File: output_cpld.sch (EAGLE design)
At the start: 40 parts, among them IC1 LM2852Y-3V3, J1 MAGJACK, U1 ONION-OMEGA2

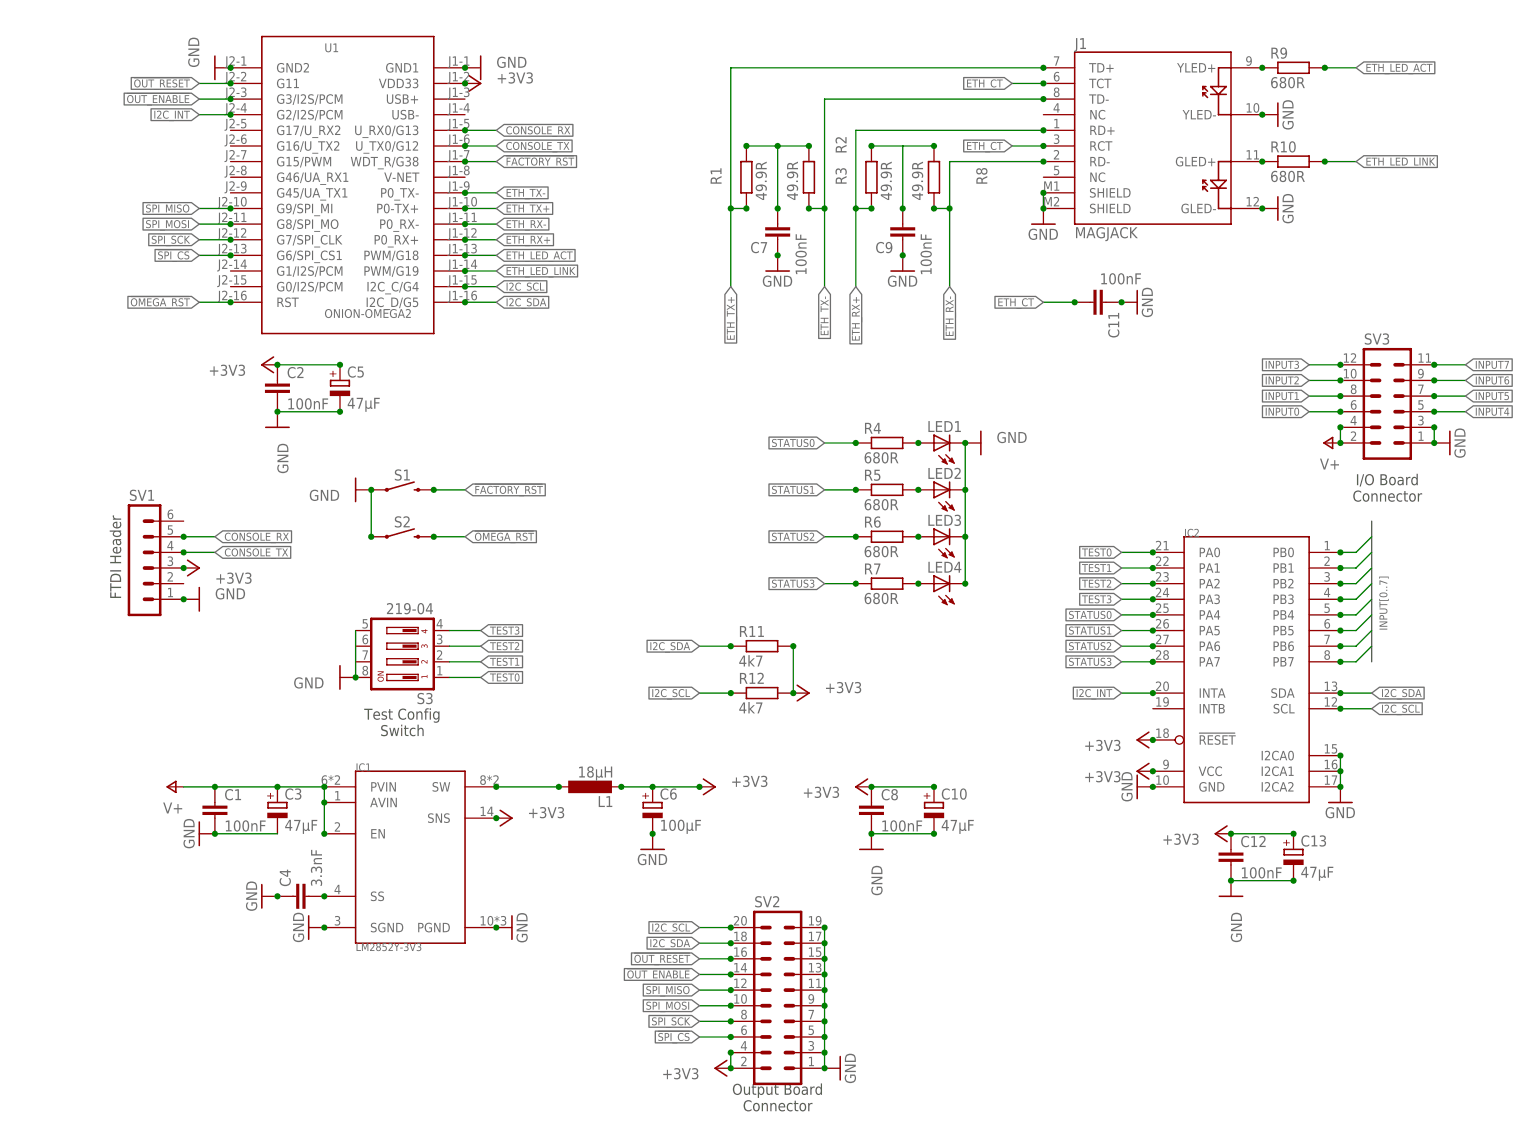
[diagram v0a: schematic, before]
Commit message: moved output CPLD to its own schematic/board
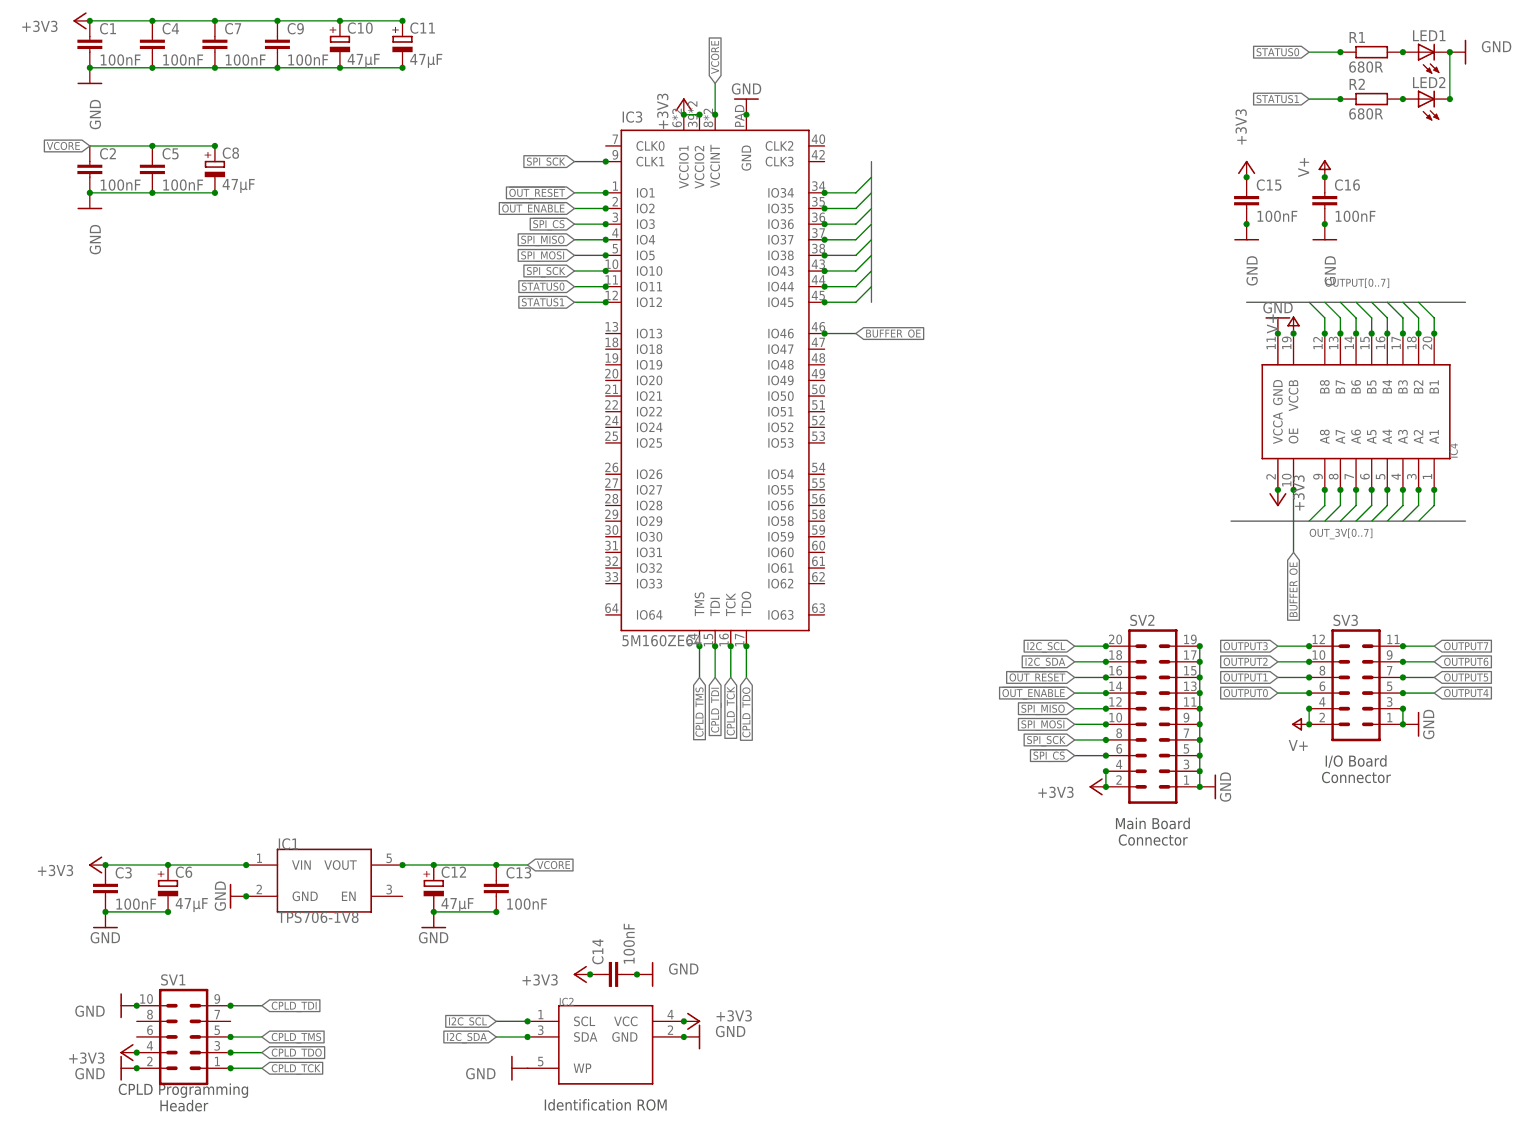
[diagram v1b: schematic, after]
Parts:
- removed J1: MAGJACK, SparkFun-Connectors:MAGJACK
- removed L1: 18µH, lichtenstein_onion:SRR1050A
- removed LED3, LED4: (no value), led:LEDCHIPLED_1206
- removed R10, R4, R5, R6, R7, R9: 680R, rcl:R-EU_M0805
- removed R11, R12: 4k7, rcl:R-EU_M0805
- removed R3, R8: 49.9R, rcl:R-EU_M0805
- removed S1, S2: MOMENTARY-SWITCH-SPST-PTH-6.0MM, SparkFun-Switches:MOMENTARY-SWITCH-SPST-PTH-6.0MM
- removed S3: 219-04, switch-dil:219-04
- removed U1: ONION-OMEGA2, lichtenstein_onion:ONION-OMEGA2
- added C14, C15, C16: 100nF, rcl:C-EUC0805
- added IC3: 5M160ZE64, lichtenstein_onion:5M160ZE64
- added IC4: (no value), lichtenstein_onion:TXB0108TSSOP20
- C11, C12, C8: value 100nF -> 47µF; device rcl:C-EUC0805 -> rcl:CPOL-EUCT6032; MOUSER (none) -> 581-NOSD107M006
- C13, C3, C5: value 47µF -> 100nF; device rcl:CPOL-EUCT6032 -> rcl:C-EUC0805; MOUSER 581-NOSD107M006 -> (none)
- C4: value 3.3nF -> 100nF
- C6: value 100µF -> 47µF; device rcl:CPOL-EUSMCD -> rcl:CPOL-EUCT6032
- IC1: value LM2852Y-3V3 -> TPS706-1V8; device lichtenstein_onion:LM2852HTSSOP14 -> lichtenstein_onion:TPS706SOT23-5
- IC2: device lichtenstein_onion:MCP23017SSOP28 -> lichtenstein_onion:AT24C02D
- R1, R2: value 49.9R -> 680R
- SV1: device con-lstb:MA06-1 -> con-lstb:MA05-2
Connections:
- removed net !FACTORY_RST: S1.2, U1.WDT_R/G38
- removed net !OMEGA_RST: S2.2, U1.RST
- removed net CONSOLE_RX: SV1.5, U1.U_RX0/G13
- removed net CONSOLE_TX: SV1.4, U1.U_TX0/G12
- removed net ETH_CT: C11.2, J1.RCT, J1.TCT
- removed net ETH_LED_ACT: R9.2, U1.PWM/G18
- removed net ETH_LED_LINK: R10.2, U1.PWM/G19
- removed net ETH_RX+: J1.RD+, R3.1, U1.P0_RX+
- removed net ETH_RX-: J1.RD-, R8.1, U1.P0_RX-
- removed net ETH_TX+: J1.TD+, R1.1, U1.P0-TX+
- removed net ETH_TX-: J1.TD-, R2.1, U1.P0_TX-
- removed net I2C_INT: IC2.INTA, U1.G2/I2S/PCM
- removed net INPUT0: IC2.PB0, SV3.6
- removed net INPUT1: IC2.PB1, SV3.8
- removed net INPUT2: IC2.PB2, SV3.10
- removed net INPUT3: IC2.PB3, SV3.12
- removed net INPUT4: IC2.PB4, SV3.5
- removed net INPUT5: IC2.PB5, SV3.7
- removed net INPUT6: IC2.PB6, SV3.9
- removed net INPUT7: IC2.PB7, SV3.11
- removed net N$10: LED3.A, R6.2
- removed net N$11: LED4.A, R7.2
- removed net N$2: LED1.A, R4.2
- removed net N$3: C7.2, R1.2, R2.2
- removed net N$4: J1.YLED+, R9.1
- removed net N$5: J1.GLED+, R10.1
- removed net N$6: C9.2, R3.2, R8.2
- removed net N$7: IC1.SW, L1.1
- removed net N$8: C4.2, IC1.SS
- removed net N$9: LED2.A, R5.2
- removed net STATUS2: IC2.PA6, R6.1
- removed net STATUS3: IC2.PA7, R7.1
- removed net TEST0: IC2.PA0, S3.1
- removed net TEST1: IC2.PA1, S3.2
- removed net TEST2: IC2.PA2, S3.3
- removed net TEST3: IC2.PA3, S3.4
- new net BUFFER_OE: IC3.IO46, IC4.OE
- new net CPLD_TCK: IC3.TCK, SV1.1
- new net CPLD_TDI: IC3.TDI, SV1.9
- new net CPLD_TDO: IC3.TDO, SV1.3
- new net CPLD_TMS: IC3.TMS, SV1.5
- new net N$13: LED1.A, R1.2
- new net N$14: LED2.A, R2.2
- new net OUTPUT0: IC4.B1, SV3.6
- new net OUTPUT1: IC4.B2, SV3.8
- new net OUTPUT2: IC4.B3, SV3.10
- new net OUTPUT3: IC4.B4, SV3.12
- new net OUTPUT4: IC4.B5, SV3.5
- new net OUTPUT5: IC4.B6, SV3.7
- new net OUTPUT6: IC4.B7, SV3.9
- new net OUTPUT7: IC4.B8, SV3.11
- new net OUT_3V0: IC3.IO34, IC4.A1
- new net OUT_3V1: IC3.IO35, IC4.A2
- new net OUT_3V2: IC3.IO36, IC4.A3
- new net OUT_3V3: IC3.IO37, IC4.A4
- new net OUT_3V4: IC3.IO38, IC4.A5
- new net OUT_3V5: IC3.IO43, IC4.A6
- new net OUT_3V6: IC3.IO44, IC4.A7
- new net OUT_3V7: IC3.IO45, IC4.A8
- new net VCORE: C12.+, C13.1, C2.1, C5.1, C8.+, IC1.VOUT, IC3.VCCINT
- net !OUT_ENABLE: now also IC3.IO2; no longer U1.G3/I2S/PCM
- net !OUT_RESET: now also IC3.IO1; no longer U1.G11
- net !SPI_CS: now also IC3.IO3; no longer U1.G6/SPI_CS1
- net +3V3: now also C1.1, C11.+, C14.1, C15.1, C3.1, C4.1, C7.1, C9.1, IC1.VIN, IC3.VCCIO1, IC3.VCCIO2, IC4.VCCA, SV1.4; no longer C12.1, C13.+, C2.1, C5.+, C8.1, IC1.SNS, IC2.!RESET, L1.2, R11.2, R12.2, SV1.3, U1.VDD33
- net GND: now also C11.-, C12.-, C13.2, C14.2, C15.2, C16.2, C3.2, C4.2, C5.2, C7.2, C8.-, C9.2, IC1.GND, IC2.WP, IC3.GND, IC4.GND, SV1.10, SV1.2; no longer C11.1, C12.2, C13.-, C3.-, C4.1, C5.-, C7.1, C8.2, C9.1, IC1.PGND, IC1.SGND, IC2.I2CA0, IC2.I2CA1, IC2.I2CA2, J1.GLED-, J1.SHIELD@0, J1.SHIELD@1, J1.YLED-, LED3.C, LED4.C, S1.1, S2.1, S3.5, S3.8, SV1.1, U1.GND1, U1.GND2
- net I2C_SCL: no longer R12.1, U1.I2C_C/G4
- net I2C_SDA: no longer R11.1, U1.I2C_D/G5
- net SPI_MISO: now also IC3.IO4; no longer U1.G9/SPI_MI
- net SPI_MOSI: now also IC3.IO5; no longer U1.G8/SPI_MO
- net SPI_SCK: now also IC3.CLK1, IC3.IO10; no longer U1.G7/SPI_CLK
- net STATUS0: now also IC3.IO11, R1.1; no longer IC2.PA4, R4.1
- net STATUS1: now also IC3.IO12, R2.1; no longer IC2.PA5, R5.1
- net V+: now also C16.1, IC4.VCCB; no longer C1.1, C3.+, IC1.AVIN, IC1.EN, IC1.PVIN
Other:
- note added: "CPLD Programming Header"
- note added: "Identification ROM"
- note added: "Main Board Connector"
- note removed: "FTDI Header"
- note removed: "Output Board Connector"
- note removed: "Test Config Switch"
- moved on the sheet: C1, C10, C2, C4, C6, C7, C9, LED1, LED2, R1, R2, SV2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

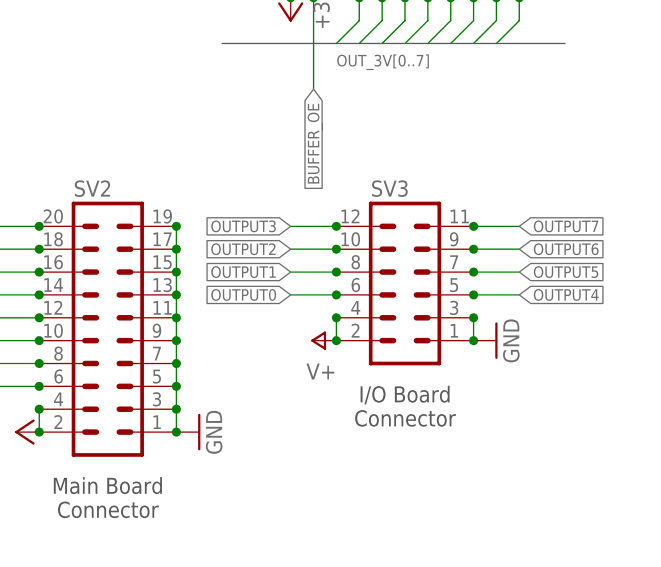
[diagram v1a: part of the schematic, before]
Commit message: Added mouser part numbers for most components
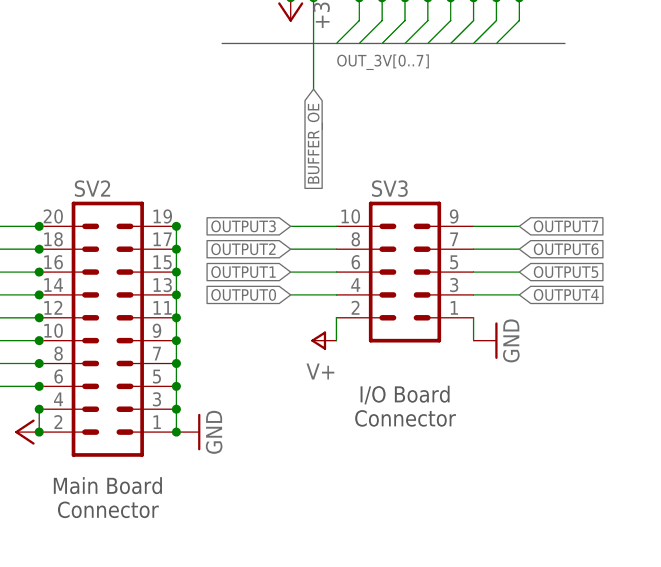
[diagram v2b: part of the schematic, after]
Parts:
- C1, C13, C14, C15, C16, C2, C3, C4, C5, C7, C9: MOUSER (none) -> 710-885012207072
- LED1, LED2: MOUSER (none) -> 604-APTR3216SGC
- R1, R2: MOUSER (none) -> 652-CR0805-FX6800GLF
- SV1: MOUSER (none) -> 517-30310-6002
- SV2: MOUSER (none) -> 517-30320-6002
- SV3: device con-lstb:MA06-2 -> con-lstb:MA05-2; MOUSER (none) -> 517-30310-6002
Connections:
- net GND: no longer SV3.3
- net OUTPUT0: now also SV3.4; no longer SV3.6
- net OUTPUT1: now also SV3.6; no longer SV3.8
- net OUTPUT2: now also SV3.8; no longer SV3.10
- net OUTPUT3: now also SV3.10; no longer SV3.12
- net OUTPUT4: now also SV3.3; no longer SV3.5
- net OUTPUT5: now also SV3.5; no longer SV3.7
- net OUTPUT6: now also SV3.7; no longer SV3.9
- net OUTPUT7: now also SV3.9; no longer SV3.11
- net V+: no longer SV3.4
